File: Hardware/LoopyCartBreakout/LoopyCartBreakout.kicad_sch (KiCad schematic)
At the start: 15 parts, among them J1 CONSOLE, J10 CON8, J11 CON9, J12 SOCKET, J2 PASSTHRU, J3 CON1, J4 CON2, J5 CON3, J6 CON4, J7 CON5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

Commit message: Fix breakout to separate VGND
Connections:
- net GND: no longer J1.7 (GND), J12.7 (GND), J2.7 (GND)
- net VGND: now reaches J11.5 (Pin_5)
- net VGND: now also J1.7 (VGND), J12.7 (VGND), J2.7 (VGND)
- no-connect marks 2 -> 1
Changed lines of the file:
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@@
   (junction (at 201.93 105.41) (diameter 0) (color 0 0 0 0)
   )
-  (no_connect (at 250.19 62.23))
   (no_connect (at 269.24 39.37))
   (wire (pts (xy 201.93 96.52) (xy 201.93 105.41))
@@
     (effects (font (size 1.27 1.27)) (justify left bottom))
   )
-  (label "GND" (at 106.68 35.56 180) (fields_autoplaced)
-    (effects (font (size 1.27 1.27)) (justify right bottom))
-  )
-  (label "GND" (at 20.32 35.56 180) (fields_autoplaced)
+  (label "VGND" (at 106.68 35.56 180) (fields_autoplaced)
+    (effects (font (size 1.27 1.27)) (justify right bottom))
+  )
+  (label "VGND" (at 20.32 35.56 180) (fields_autoplaced)
     (effects (font (size 1.27 1.27)) (justify right bottom))
   )
@@
     (effects (font (size 1.27 1.27)) (justify right bottom))
   )
-  (label "GND" (at 63.5 35.56 180) (fields_autoplaced)
+  (label "VGND" (at 63.5 35.56 180) (fields_autoplaced)
     (effects (font (size 1.27 1.27)) (justify right bottom))
   )
@@
     (effects (font (size 1.27 1.27)) (justify right bottom))
   )
+  (label "VGND" (at 250.19 62.23 180) (fields_autoplaced)
+    (effects (font (size 1.27 1.27)) (justify right bottom))
+  )

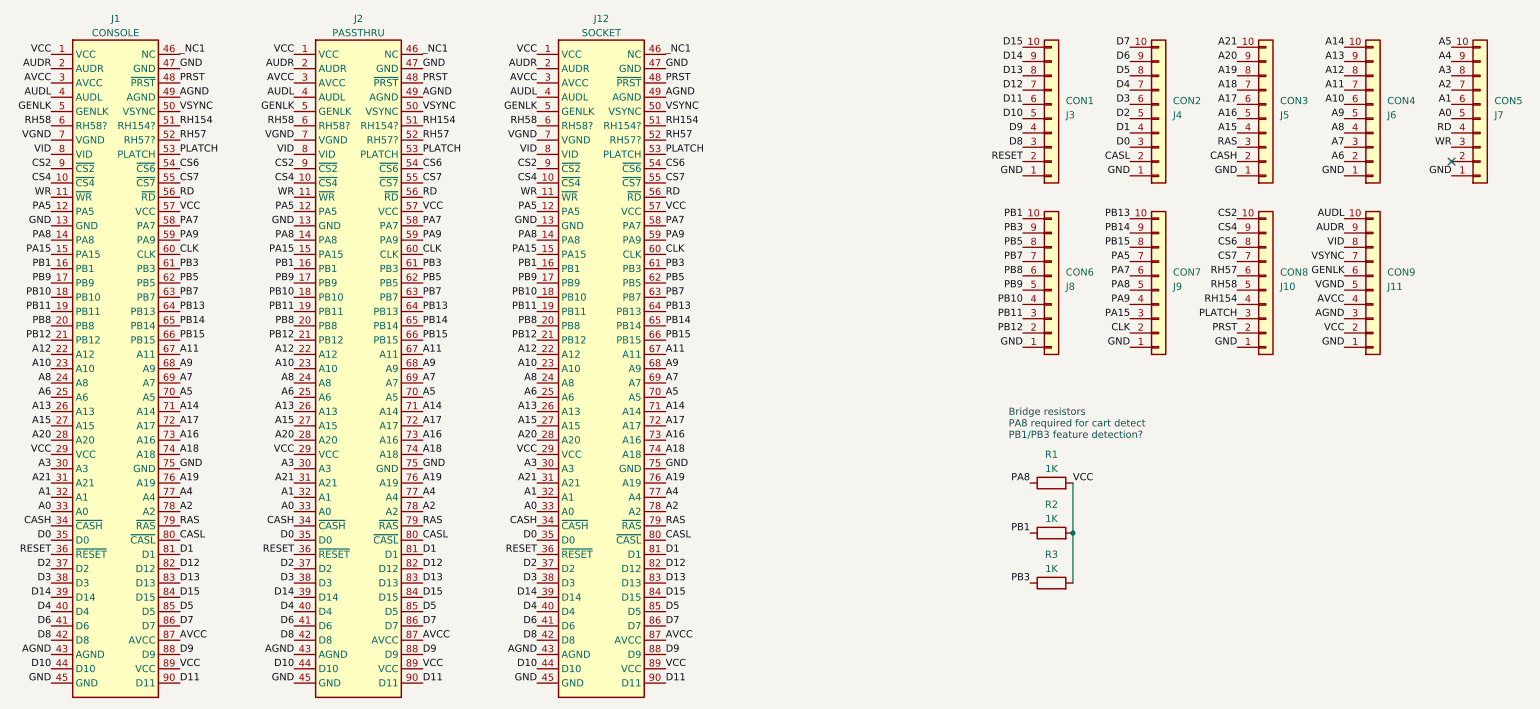
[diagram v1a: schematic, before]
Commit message: Update cart breakout board & treat kicad files as binary
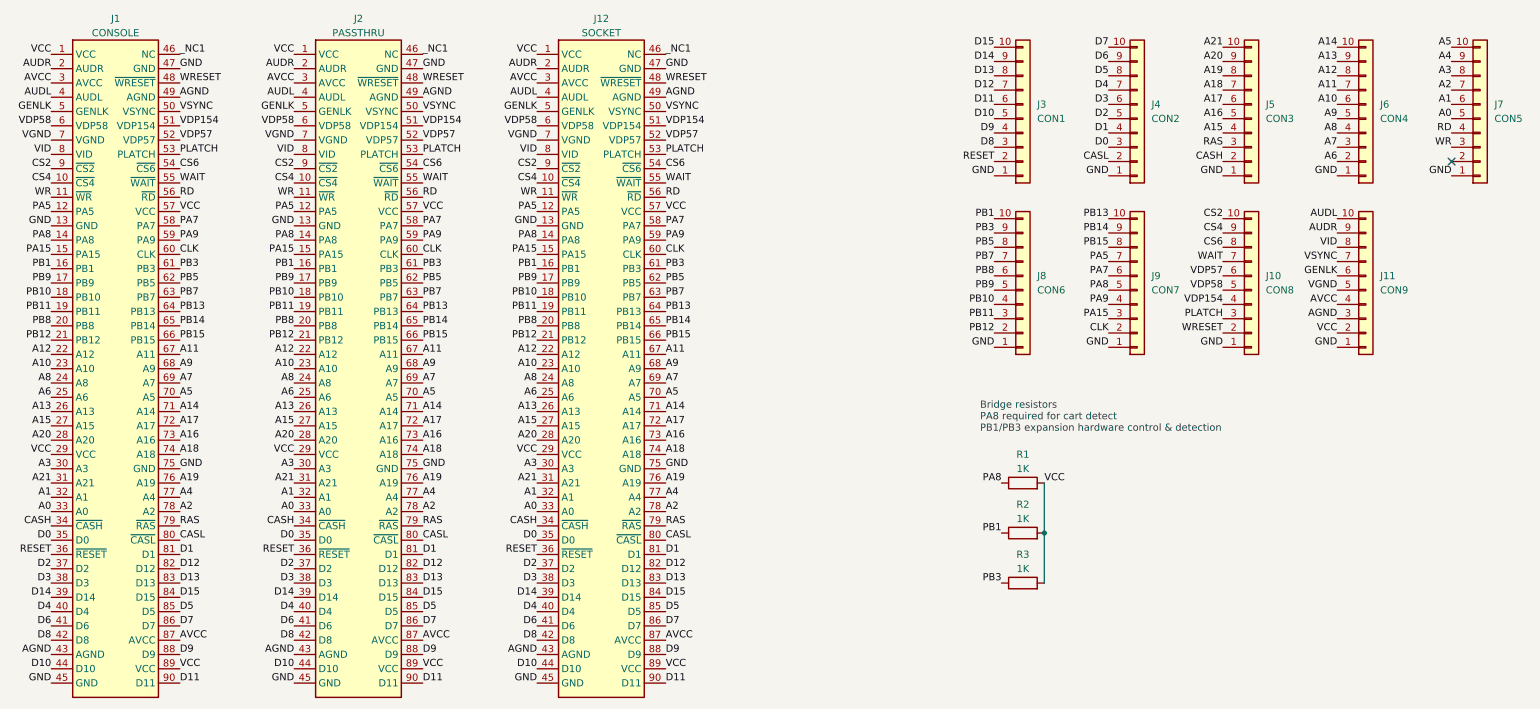
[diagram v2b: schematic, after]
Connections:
- net CS7 renamed WAIT
- net PRST renamed WRESET
- net RH154 renamed VDP154
- net RH57 renamed VDP57
- net RH58 renamed VDP58
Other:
- note added: "Bridge resistors PA8 required for cart detect PB1/PB3 expansion hardware control & detection"
- note removed: "Bridge resistors PA8 required for cart detect PB1/PB3 feature detection?"
- moved on the sheet: J10, J11, J3, J4, J5, J6, J8, J9, R1, R2, R3
